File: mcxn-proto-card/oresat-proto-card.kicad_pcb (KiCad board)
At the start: 4 copper layers, 99.8 x 94.6 mm, 140 parts, among them J1 J-SAMTEC-TFM-120-X1-XXX-D-RA, J10 61083-061409LF, J11 436500201, J14 ESQ-126-12-G-D, J15 ESQ-126-12-G-D, J3 SM14B-SHLS-TF, Q1 DMP2240UDM, Q2 DMP3050LVT-7, Q7 DMP3050LVT-7, Q8 PMV45EN, Q9 PMV45EN, U1 MCXN947VKLT, U10 TPS62111RSA, U11 MIC842LYC5, U12 MIC842LYC5, U2 MAX7310, U3 TS5A21366DCUR, U6 MAX4211FETE, U8 TCAN330, Y2 24 MHz

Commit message: ADjusted J14 and J15 placement for piPlasma alignment. Added ESI logo.
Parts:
- added G***: LOGO, LOGO, F.Cu at (172.1, 139.4)
- moved J14 2.55 mm to (182.4, 73.5)
- moved J15 2.55 mm to (187.5, 73.5)
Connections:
- U10 pad 17: +3.3V -> GND
- U11 pad 2: +3.3V -> GND
- U2 pad 17: +3.3V -> GND
- U6 pad 17: +3.3V -> GND
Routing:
- net /CAN1_H: track 1.27 -> 10.7 mm
- net /CAN1_L: track 1.51 -> 8.01 mm
- net /SPARE22: track 0.04 -> 6.04 mm
- net /Microcontroller/CDH_COMM_TX: track 199.7 -> 197.4 mm
- net GND: track 0.00 -> 1.42 mm, vias 311 -> 258
- net +3.3V: track 44.7 -> 44.9 mm, vias 53 -> 46

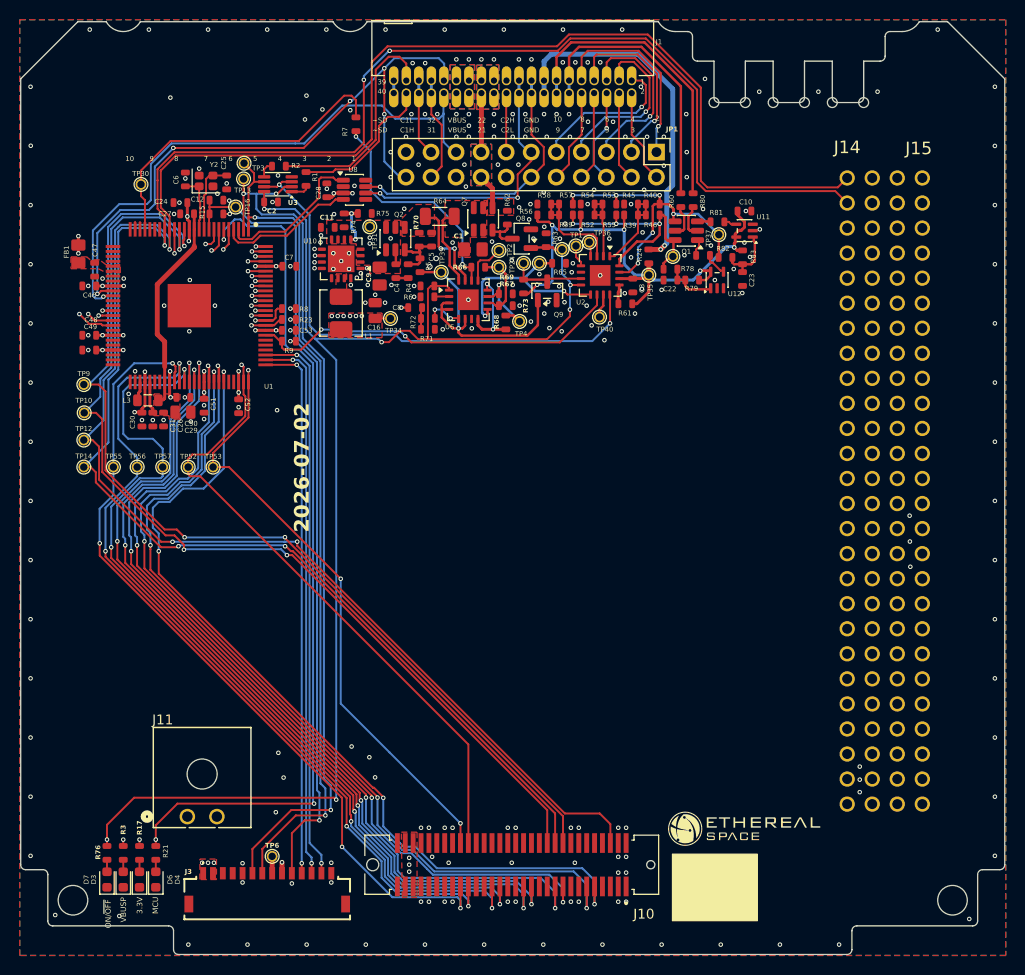
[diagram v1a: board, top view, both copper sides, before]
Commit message: Added mounting holes for piPlasma
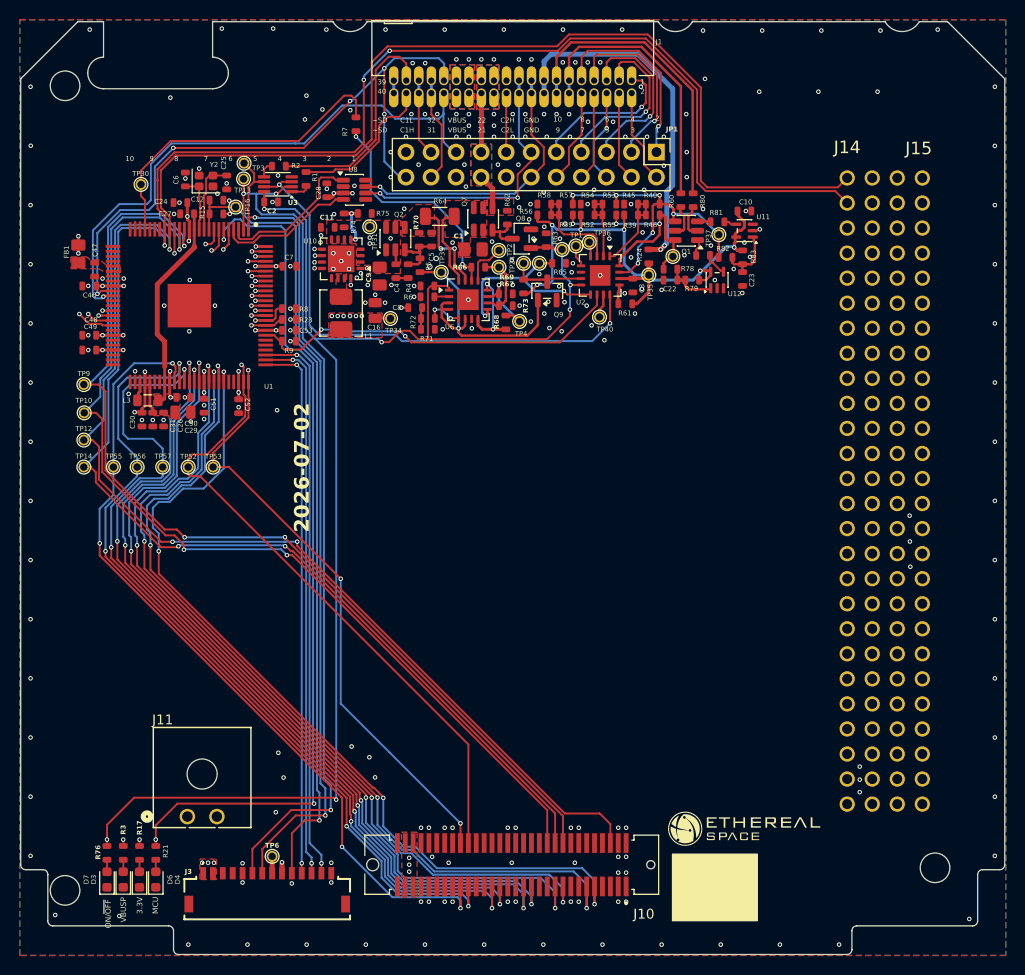
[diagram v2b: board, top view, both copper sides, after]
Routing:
- net GND: vias 258 -> 261
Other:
- outline, holes or cut-outs redrawn

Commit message: Adjusted RF connection
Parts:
- moved J10 0.61 mm to (148.5, 142.6)
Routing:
- net /Microcontroller/P3_13: track 85.7 -> 84.7 mm
- net /Microcontroller/P3_14: track 84.4 -> 83.5 mm
- net /Microcontroller/P3_15: track 90.9 -> 90.1 mm
- net /Microcontroller/P3_11: track 89.4 -> 88.7 mm
- net /Microcontroller/P3_8: track 89.7 -> 89.1 mm
- net GND: vias 261 -> 260
